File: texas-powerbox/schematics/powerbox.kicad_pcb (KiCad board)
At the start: 2 copper layers, 94 x 68.6 mm, 35 parts, among them J1 BATTERY, J2 ADAPTER, J3 USB_STACKED, J4 USB_STACKED, J7 5V, J8 24V, K1 J107F1CS1224VDC.36, Q1 AOD417, U1 LM22673-5.0

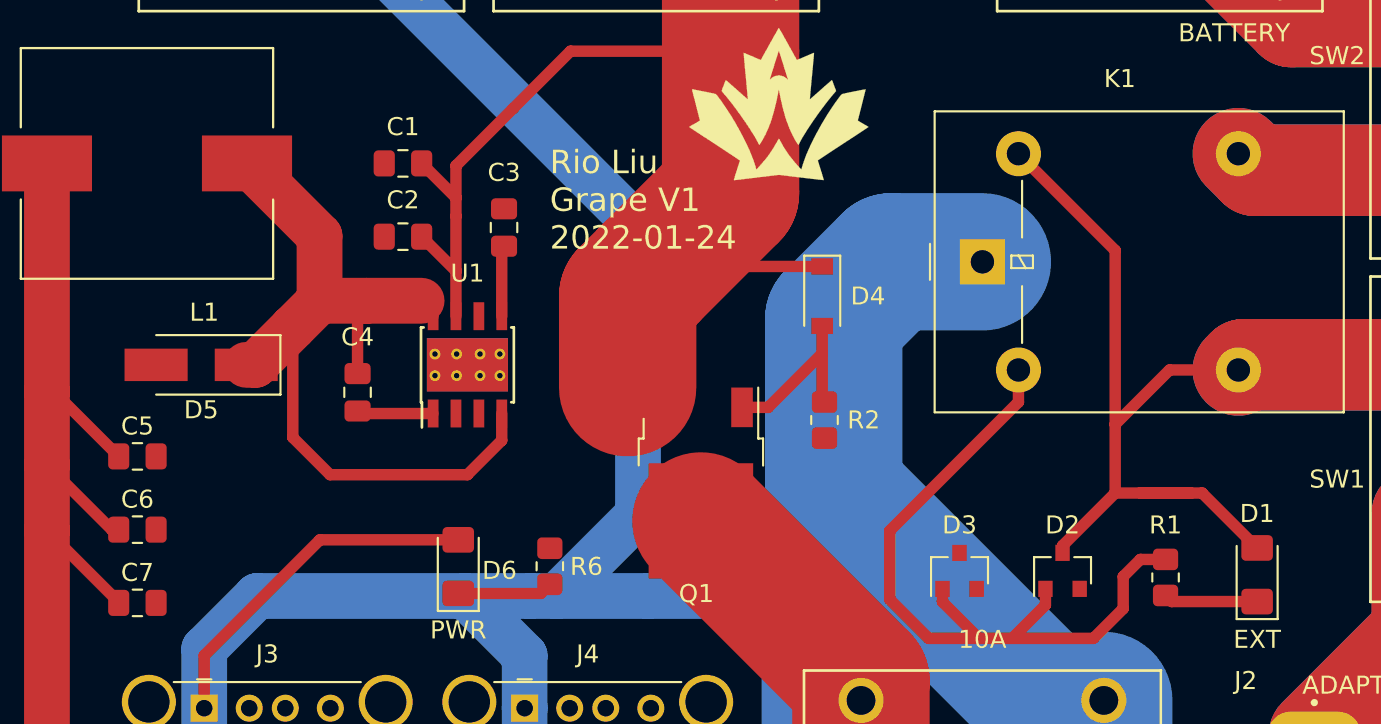
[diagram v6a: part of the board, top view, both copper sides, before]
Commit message: ground the bulk converter better and updater gerbers
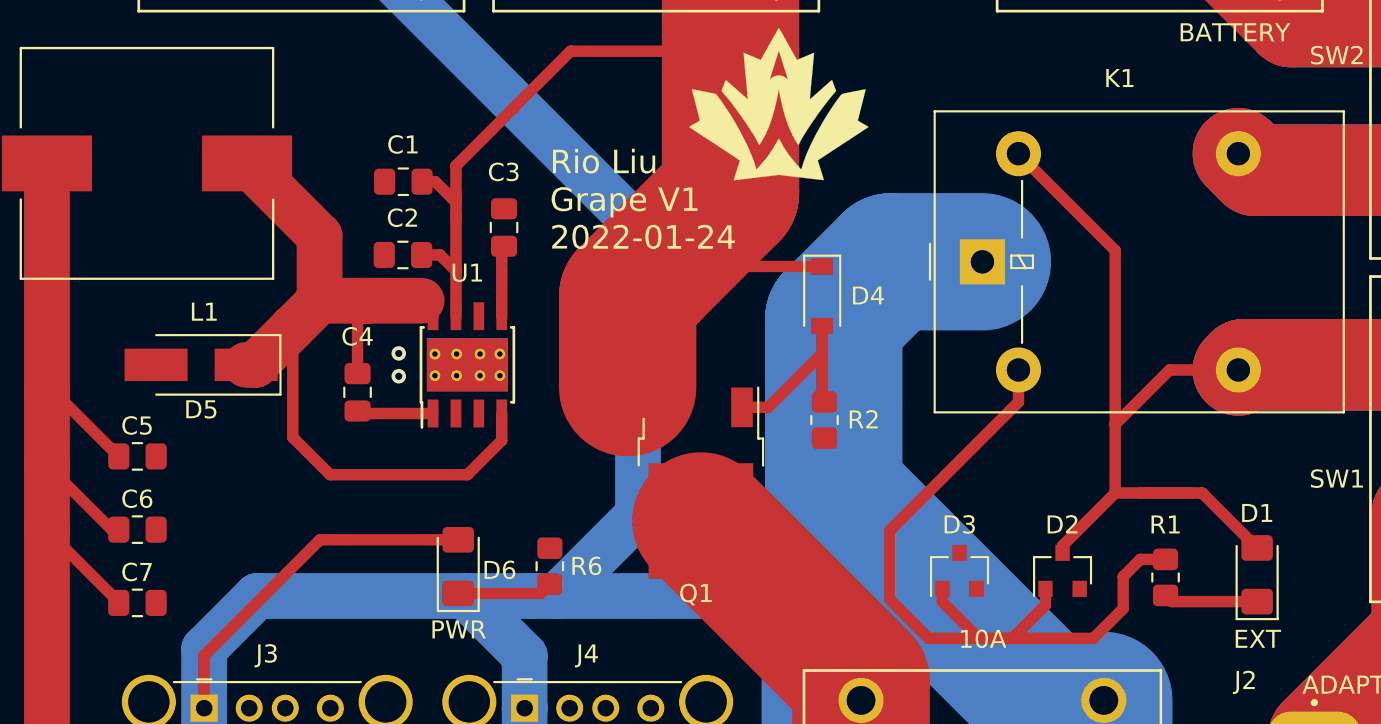
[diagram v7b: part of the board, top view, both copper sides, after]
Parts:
- moved C1 1.02 mm to (133.6, 114.3)
- moved C2 1.02 mm to (133.6, 118.4)
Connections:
- U1 pad 9: (no net) -> GND
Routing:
- net +24V: track 66.1 -> 65.3 mm
- net GND: vias 0 -> 2

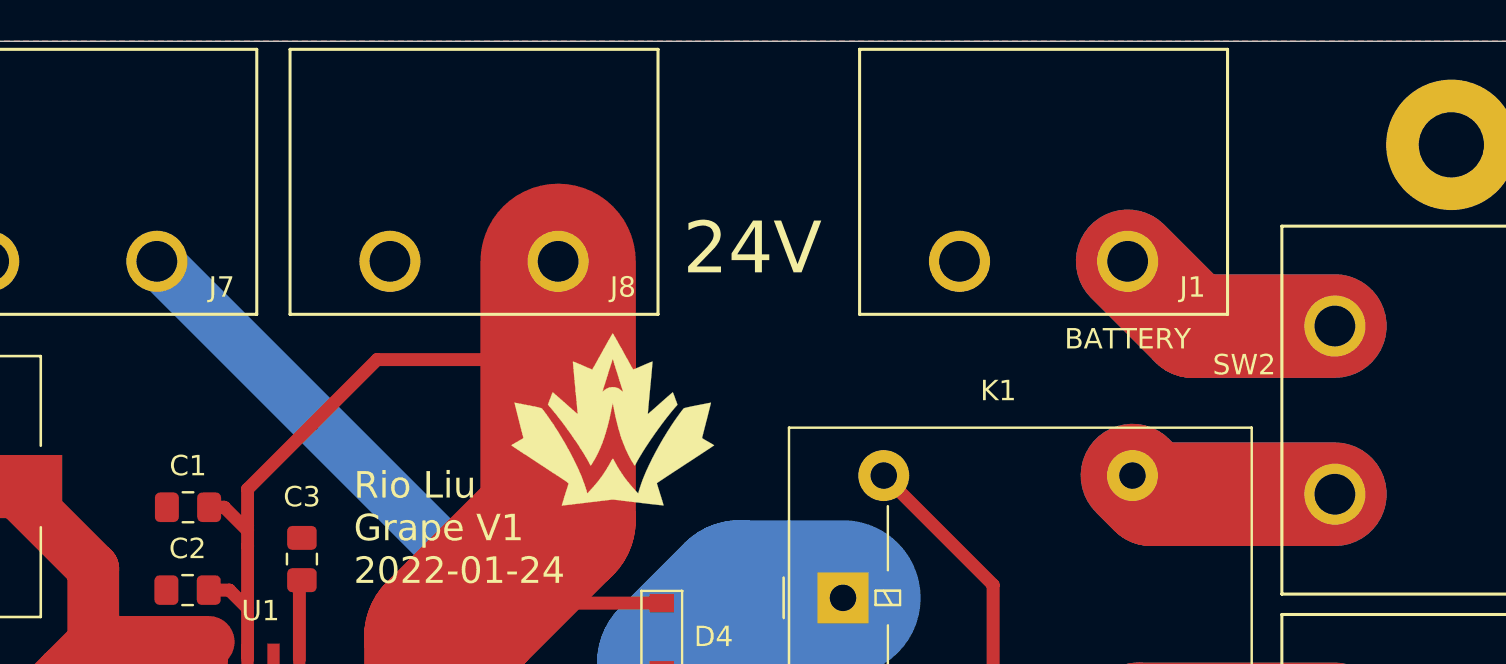
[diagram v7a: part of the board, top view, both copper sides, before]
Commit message: add polarity silkscreen and update gerbers
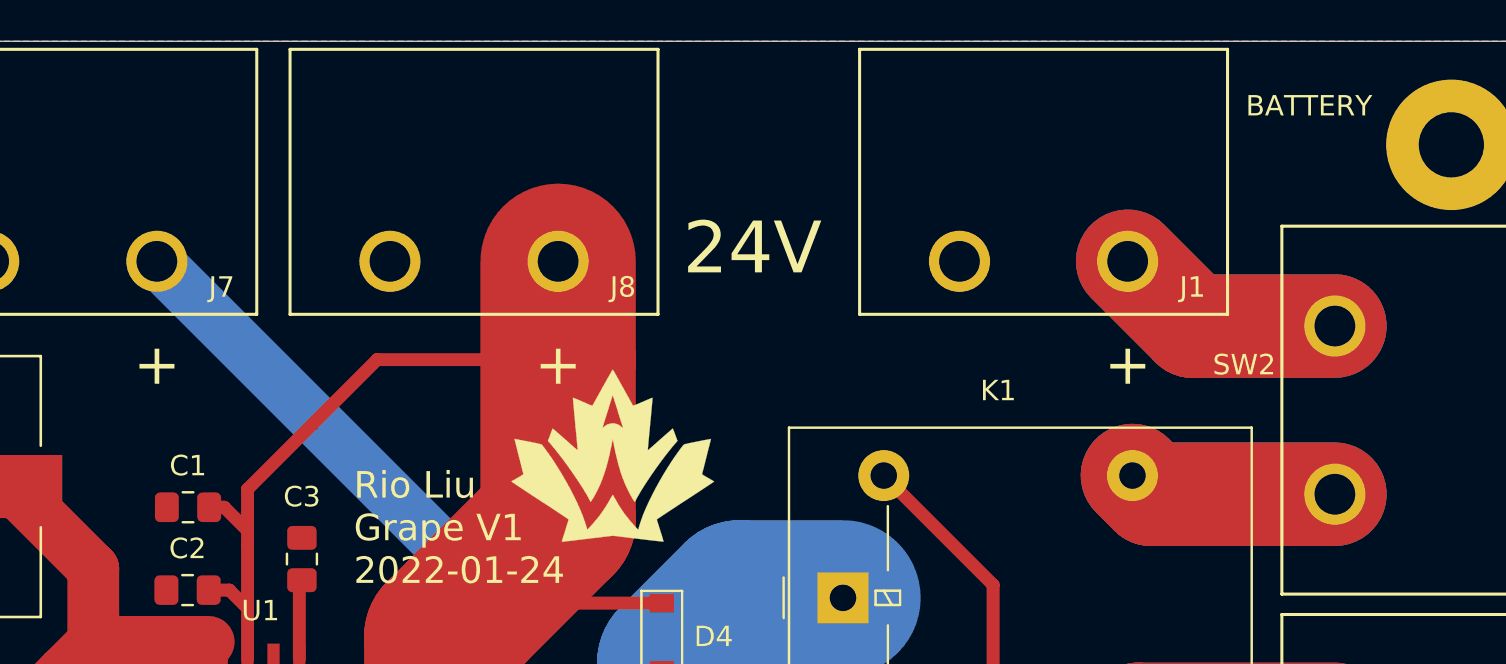
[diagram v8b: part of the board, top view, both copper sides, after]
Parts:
- moved G*** 1.78 mm to (154.4, 111.8)
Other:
- board text added: "+"
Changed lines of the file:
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@@
       (effects (font (size 1 1) (thickness 0.15)))
     )
-    (fp_text value "BATTERY" (at 8.255 3.81) (layer "F.SilkS")
+    (fp_text value "BATTERY" (at 17.145 -7.62) (layer "F.SilkS")
       (effects (font (size 1 1) (thickness 0.15)))
     )
@@
   )
   (footprint "Team_Logo:Logo_SilkScreen_10mm" (layer "F.Cu")
-    (at 154.432 109.982)
+    (at 154.432 111.76)
     (attr through_hole)
     (fp_text reference "G***" (at 0 0) (layer "F.SilkS") hide
@@
   (gr_line (start 200.66 91.44) (end 200.66 160.02) (layer "Edge.Cuts") (width 0.05))
   (gr_line (start 200.66 160.02) (end 106.68 160.02) (layer "Edge.Cuts") (width 0.05))
+  (gr_text "+" (at 151.765 107.315) (layer "F.SilkS")
+    (effects (font (size 2 2) (thickness 0.3)))
+  )
+  (gr_text "+" (at 179.705 107.315) (layer "F.SilkS")
+    (effects (font (size 2 2) (thickness 0.3)))
+  )
+  (gr_text "+" (at 132.08 107.315) (layer "F.SilkS")
+    (effects (font (size 2 2) (thickness 0.3)))
+  )
   (gr_text "Rio Liu\nGrape V1\n2022-01-24" (at 141.732 115.316) (layer "F.SilkS")
     (effects (font (size 1.3 1.3) (thickness 0.3)) (justify left))
